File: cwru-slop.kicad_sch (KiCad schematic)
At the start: 24 parts, among them SW1 SW_SPDT, U1 TLV9001IDCK, U2 AP63205WU, U3 TLV75533PDBV, U4 STM32L433CCTx, U5 TPS2116DRL

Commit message: add accelerometer
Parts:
- added C16: 0.1u, Capacitor_SMD:C_0603_1608Metric_Pad1.08x0.95mm_HandSolder, symbol slopp:C
- added C17: 1.0u, Capacitor_SMD:C_0603_1608Metric_Pad1.08x0.95mm_HandSolder, symbol slopp:C
- added R2, R3: 4.7k, Resistor_SMD:R_0603_1608Metric_Pad0.98x0.95mm_HandSolder, symbol slopp:R
- added U6: FXLS8974CFR3, SYS27_Footprints:DFN10_2X2_STM, symbol slopp:FXLS8974CFR3
- C9: value 100n -> 0.1u
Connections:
- net GND is gone; now on net +3V3: C1.2, C10.2, C12.2, C13.1, C14.2, C15.2, C2.2, C3.2, C4.2, C5.2, C6.2, C7.2, C8.2, C9.1, SW1.1 (A), U2.4 (GND), U3.2 (GND), U4.23 (VSS), U4.35 (VSS), U4.47 (VSS), U4.8 (VSSA), U5.1 (GND)
- net +3V3: now also C16.1, C16.2, C17.1, C17.2, R2.2, R3.2, U6.1 (VDD), U6.10 (GND), U6.2 (BT_MODE), U6.9 (INTF_SEL)
- net +5V: no longer C12.1, C13.2, L1.2, U2.1 (FB), U5.3 (VIN1), U5.5 (MODE), U5.6 (VIN2)
- net ACCEL_SCL: now reaches U4.30 (PA9)
- net ACCEL_SCL: now also R2.1, U6.5 (SCL/SCLK)
- net ACCEL_SDA: now reaches U4.31 (PA10)
- net ACCEL_SDA: now also R3.1, U6.4 (SDA/SPI_MOSI/SPI_DATA)
- net BUCK_BST renamed BUCK_SW
- new net +5V_PWR: C12.1, C13.2, L1.2, U2.1 (FB), U5.3 (VIN1), U5.5 (MODE)
- new net +5V_USB: U5.6 (VIN2)
- no-connect marks 0 -> 4
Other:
- note added: "3V3 LDO"
- note added: "5V BUCK"
- note added: "5V PWR MUX"
- note added: "Accelerometer"
- note added: "POWER!"
- moved on the sheet: C10, C11, C12, C13, C14, C15, C9, L1, SW1, U1, U2, U3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

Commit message: can trans + esd prot
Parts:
- added C18, C19: 0.1u, Capacitor_SMD:C_0603_1608Metric_Pad1.08x0.95mm_HandSolder, symbol slopp:C
- added U7: ESDCAN24-2BLY, SYS27_Footprints:SOT_24-2BLY_STM, symbol slopp:ESDCAN24-2BLY
- added U8: MCP2562-E-SN, Package_SO:SOIC-8_3.9x4.9mm_P1.27mm, symbol slopp:MCP2562-E-SN
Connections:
- net +3.3V: now also C19.2, U8.5 (Vio)
- net +3V3: now also C18.2, C19.1, U7.3, U8.2 (VSS)
- net +5V: now also C18.1, U8.3 (VDD)
- net CAN_RXD: now reaches U4.32 (PA11)
- net CAN_RXD: now also U8.4 (RXD)
- net CAN_TXD: now reaches U4.33 (PA12)
- net CAN_TXD: now also U8.1 (TXD)
- net CAN_STBY: now reaches U4.34 (PA13)
- net CAN_STBY: now also U8.8 (STBY)
- new net: U7.2, U8.6 (CANL)
- new net: U7.1, U8.7 (CANH)
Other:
- note added: "CAN Transciever (to bus)"
- moved on the sheet: C16, C17, C8, FB1, R2, R3, U6

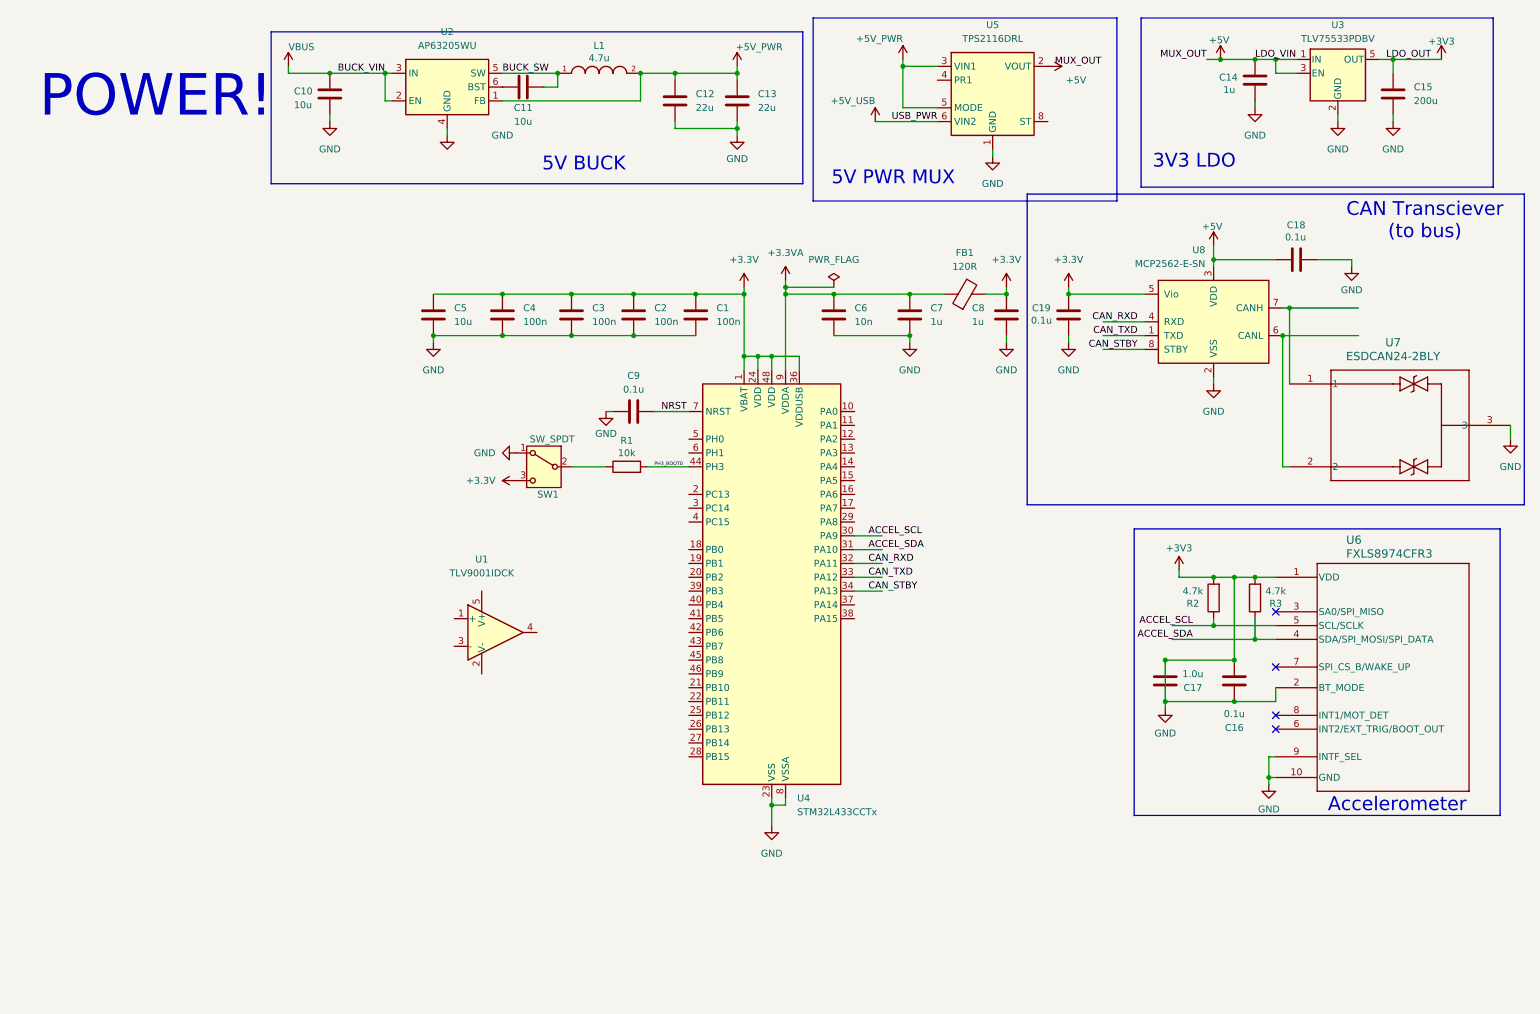
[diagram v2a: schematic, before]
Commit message: add eeprom and crystal
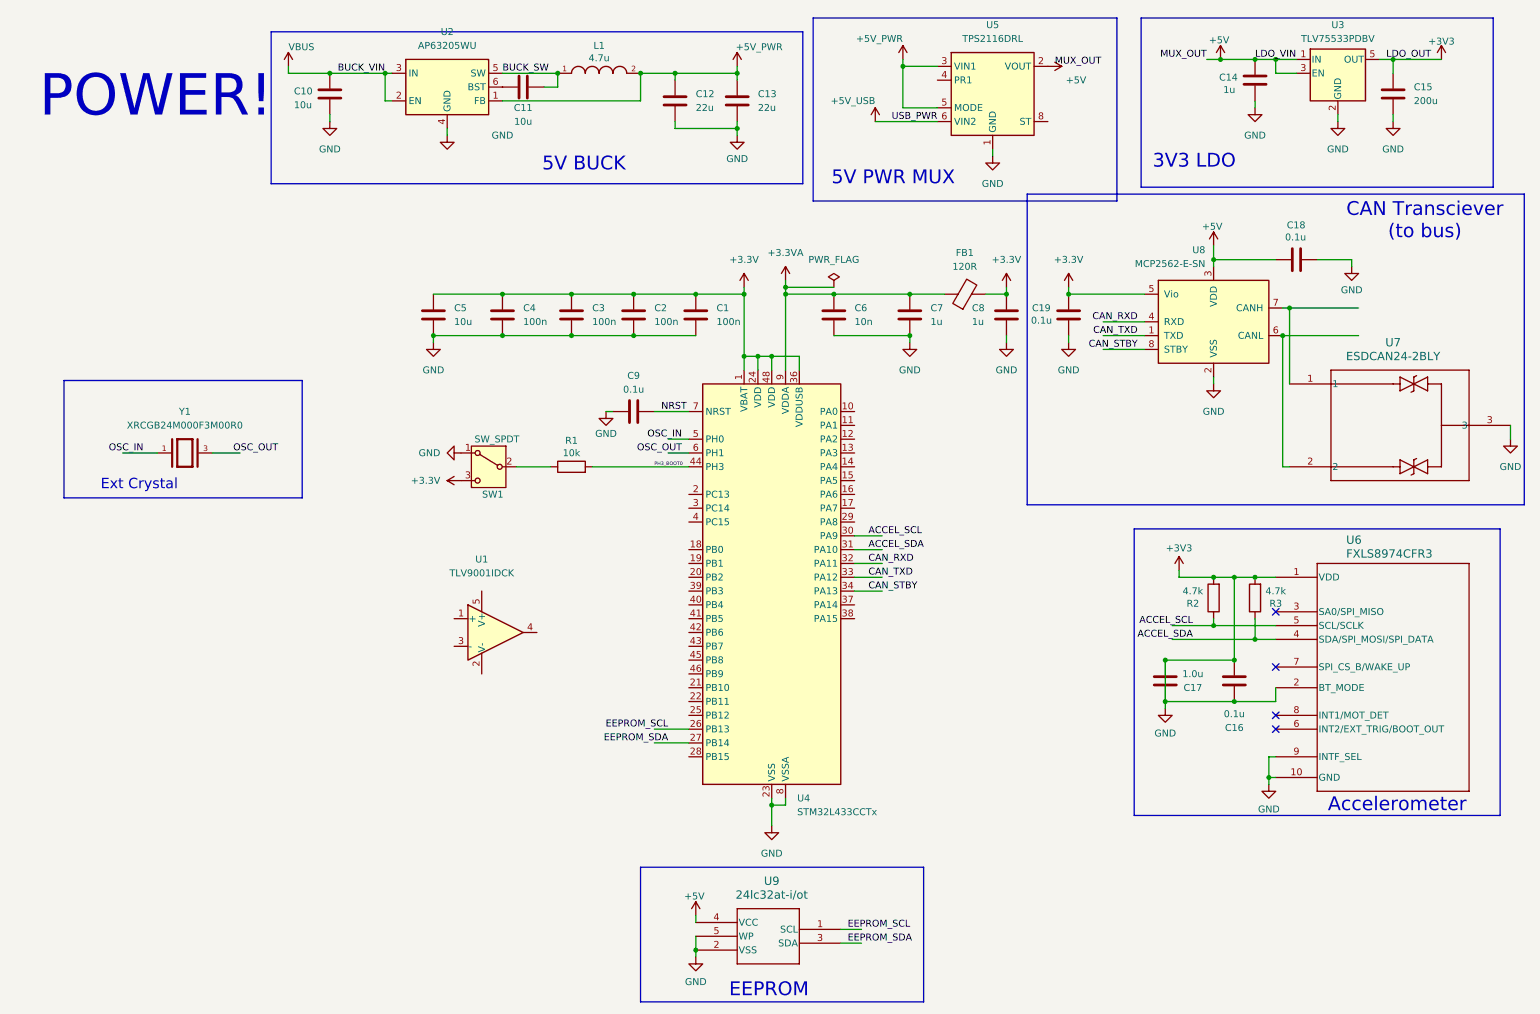
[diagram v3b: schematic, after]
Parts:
- added U9: 24lc32at-i/ot, SYS27_Footprints:SOT-24-5_MC_MCH, symbol slopp:24lc32at-i_ot
- added Y1: XRCGB24M000F3M00R0, SYS27_Footprints:OSC_XRCGB24M000F3M00R0, symbol slopp:XRCGB24M000F3M00R0
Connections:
- net +3V3: now also U9.2 (VSS), U9.5 (WP)
- net +5V: now also U9.4 (VCC)
- net EEPROM_SCL: now reaches U4.26 (PB13)
- net EEPROM_SCL: now also U9.1 (SCL)
- net EEPROM_SDA: now reaches U4.27 (PB14)
- net EEPROM_SDA: now also U9.3 (SDA)
- net OSC_IN: now reaches U4.5 (PH0)
- net OSC_IN: now also Y1.1
- net OSC_OUT: now reaches U4.6 (PH1)
- net OSC_OUT: now also Y1.3
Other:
- note added: "EEPROM"
- note added: "Ext Crystal"
- moved on the sheet: R1, SW1

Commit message: reorg i/o sides, add reset button
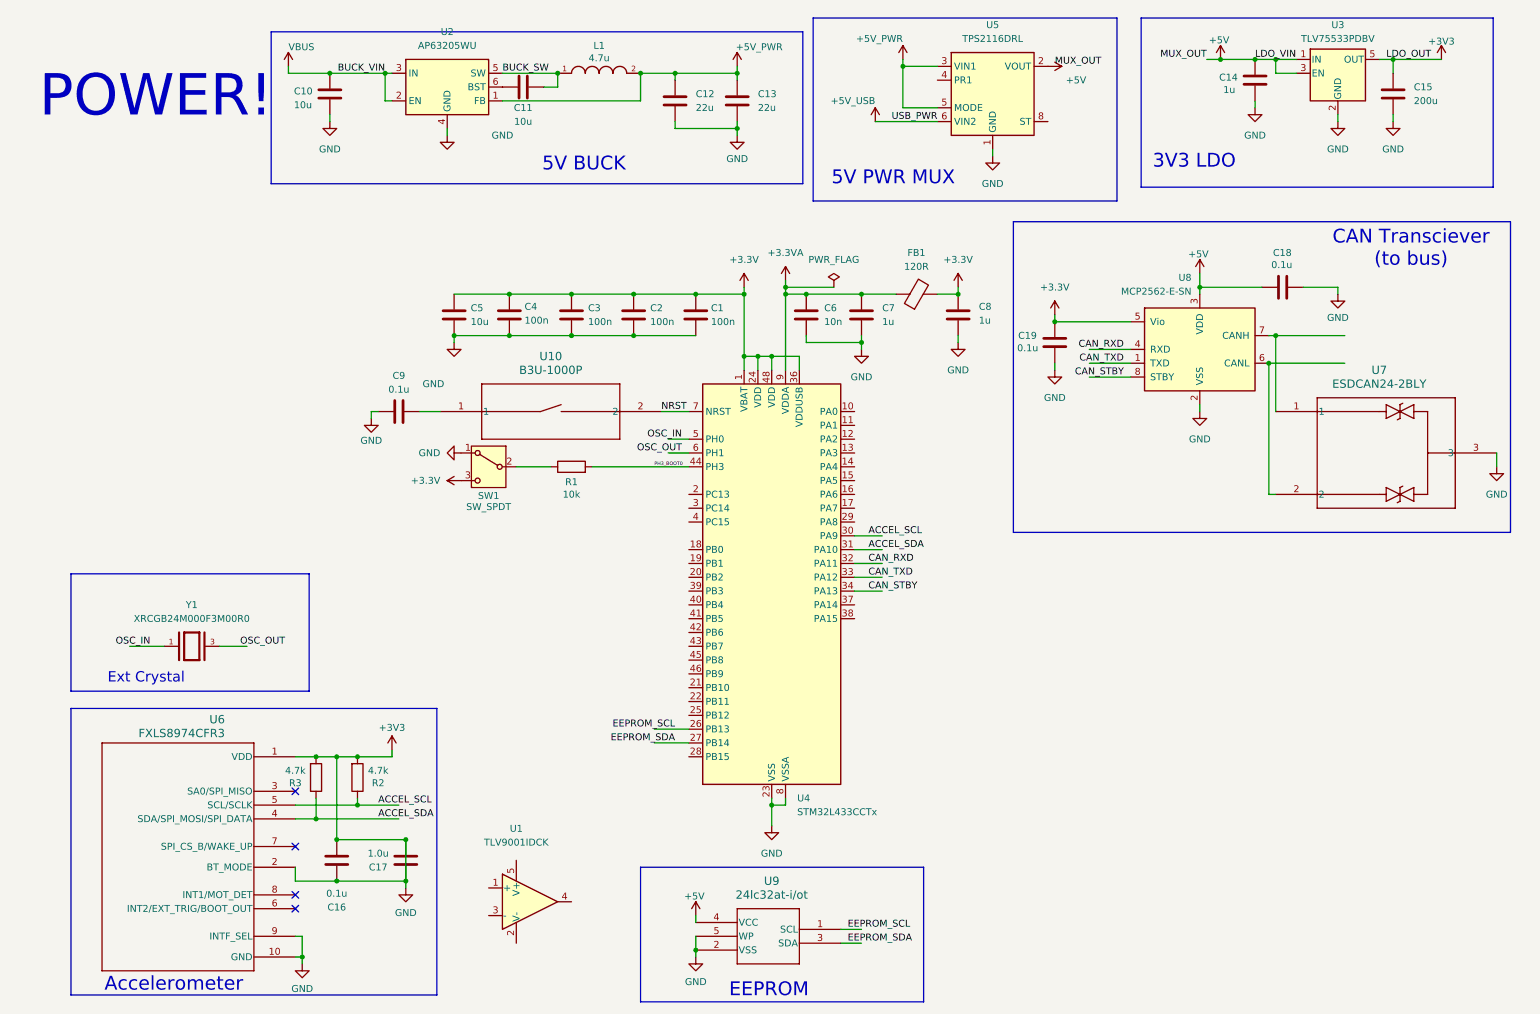
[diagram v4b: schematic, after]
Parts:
- added U10: B3U-1000P, SYS27_Footprints:B3U-1000P, symbol slopp:B3U-1000P
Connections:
- net NRST: now also U10.2; no longer C9.2
- new net: C9.2, U10.1
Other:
- moved on the sheet: C16, C17, C18, C19, C4, C5, C6, C7, C8, C9, FB1, R2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

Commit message: add usb-c 2.0 conn
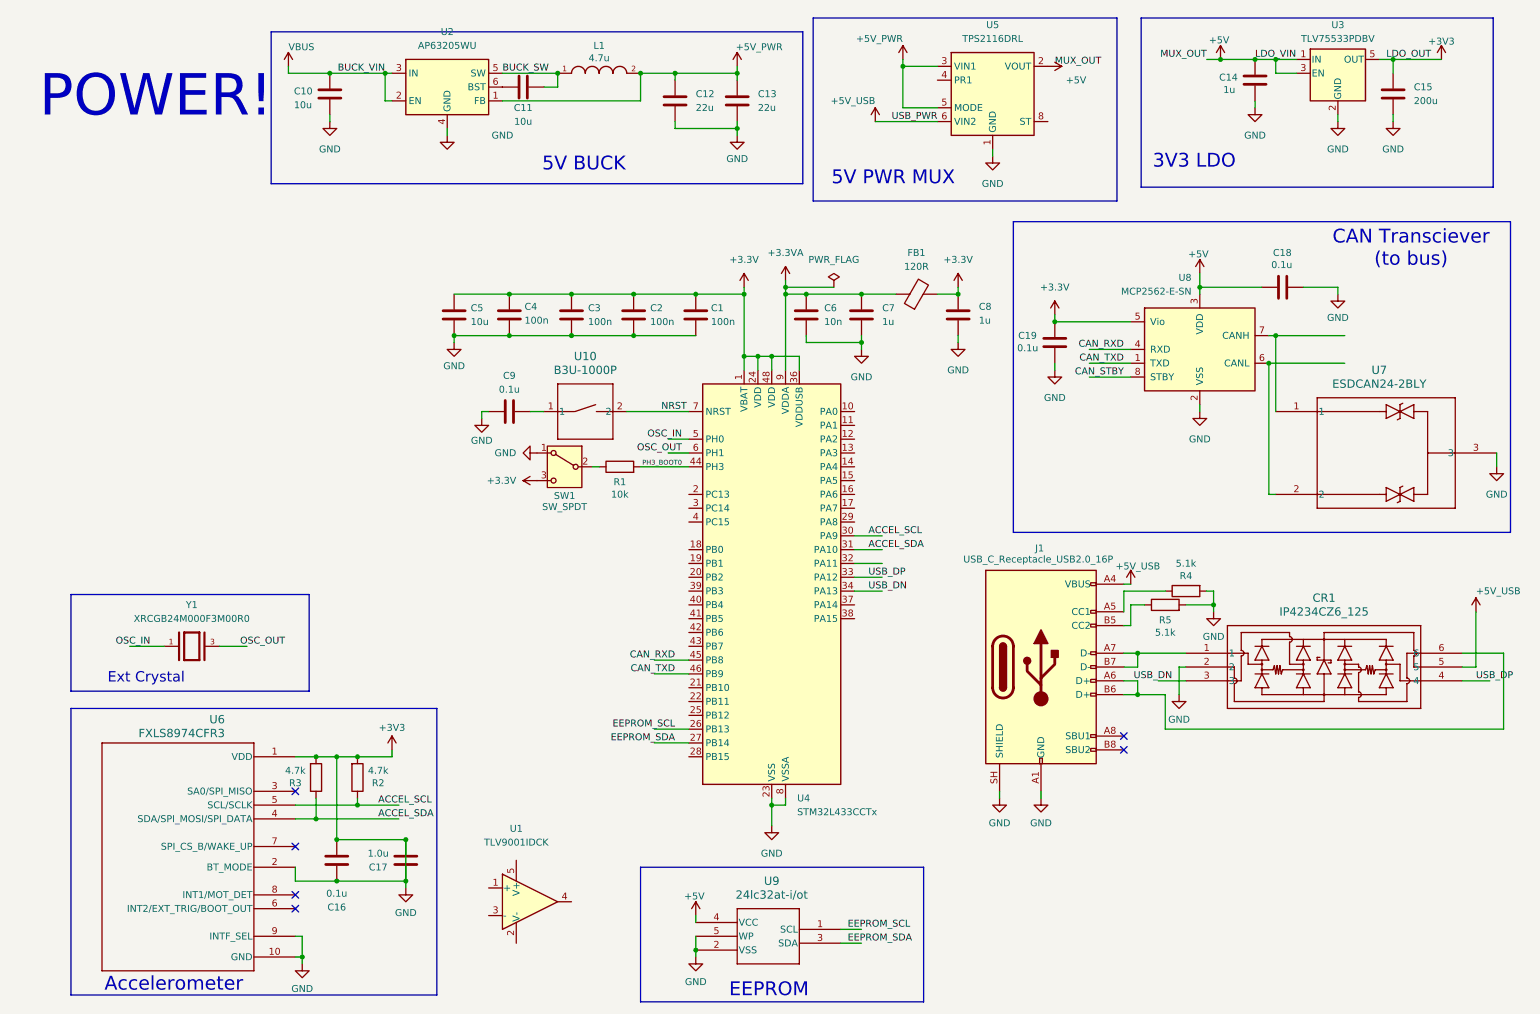
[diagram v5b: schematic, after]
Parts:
- added CR1: IP4234CZ6_125, SYS27_Footprints:TSOP6_SOT457_NEX, symbol slopp:IP4234CZ6_125
- added J1: USB_C_Receptacle_USB2.0_16P, SYS27_Footprints:B3U-1000P, symbol Connector:USB_C_Receptacle_USB2.0_16P
- added R4, R5: 5.1k, Resistor_SMD:R_0603_1608Metric_Pad0.98x0.95mm_HandSolder, symbol slopp:R
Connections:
- net +3V3: now also CR1.2, J1.A1 (GND), J1.A12 (GND), J1.B1 (GND), J1.B12 (GND), J1.SH (SHIELD), R4.2, R5.2
- net +5V_USB: now also CR1.5, J1.A4 (VBUS), J1.A9 (VBUS), J1.B4 (VBUS), J1.B9 (VBUS)
- net CAN_RXD: now also U4.45 (PB8); no longer U4.32 (PA11)
- net CAN_STBY: no longer U4.34 (PA13)
- net CAN_TXD: now also U4.46 (PB9); no longer U4.33 (PA12)
- new net: CR1.1, J1.A7 (D-), J1.B7 (D-)
- new net: CR1.6, J1.A6 (D+), J1.B6 (D+)
- new net: J1.B5 (CC2), R5.1
- new net: J1.A5 (CC1), R4.1
- new net USB_DN: CR1.3, U4.34 (PA13)
- new net USB_DP: CR1.4, U4.33 (PA12)
- no-connect marks 4 -> 6
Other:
- moved on the sheet: C9, R1, SW1, U10

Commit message: rotate usb diode, org
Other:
- note added: "USB w/ ESD"
- moved on the sheet: C1, C16, C17, C18, C19, C2, C3, C4, C5, C6, C7, C8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

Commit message: connect transciever stby to mcu
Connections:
- net CAN_STBY: now also U4.21 (PB10)
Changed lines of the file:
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@@
+	(wire
+		(pts
+			(xy 152.4 132.08) (xy 158.75 132.08)
+		)
+		(stroke
+			(width 0)
+			(type default)
+		)
+	)
 	(wire
 		(pts
@@
 		)
 	)
+	(label "CAN_STBY"
+		(at 156.21 132.08 180)
+		(effects
+			(font
+				(size 1.27 1.27)
+			)
+			(justify right bottom)
+		)
+	)

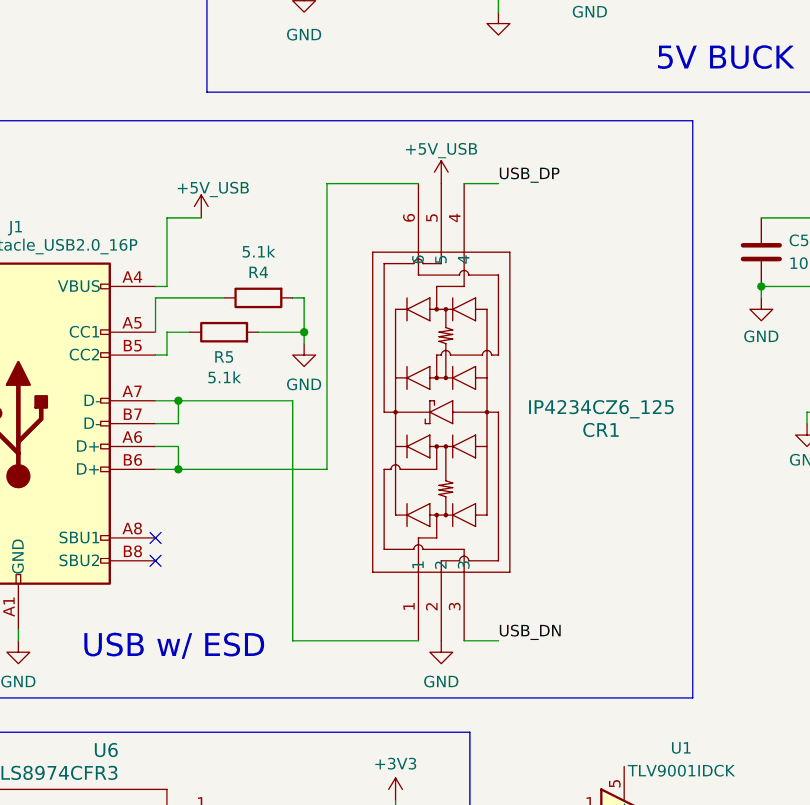
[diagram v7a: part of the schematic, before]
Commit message: reroute usb -> esd less confusingly
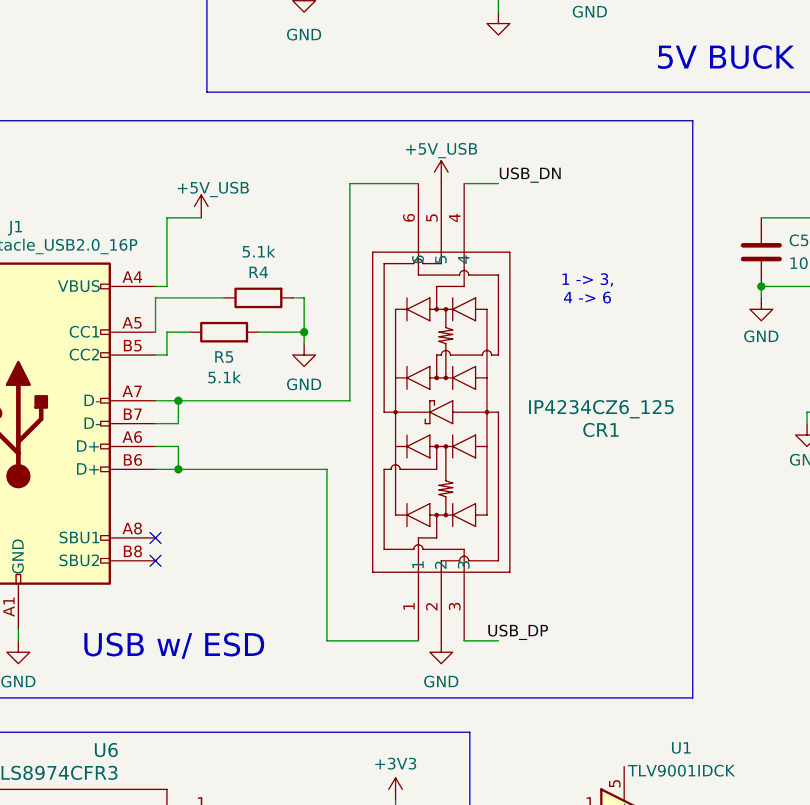
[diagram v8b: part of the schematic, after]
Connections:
- net USB_DN: now also CR1.4; no longer CR1.3
- net USB_DP: now also CR1.3; no longer CR1.4
- net at J1.A7 (D-), J1.B7 (D-): now also CR1.6; no longer CR1.1
- net at J1.A6 (D+), J1.B6 (D+): now also CR1.1; no longer CR1.6
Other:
- note added: "1 -> 3, 4 -> 6"
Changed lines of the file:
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@@
+		)
+	)
+	(text "1 -> 3,\n4 -> 6"
+		(exclude_from_sim no)
+		(at 96.266 67.818 0)
+		(effects
+			(font
+				(size 1.27 1.27)
+			)
 		)
 	)
@@
 	(wire
 		(pts
+			(xy 69.85 80.01) (xy 69.85 55.88)
+		)
+		(stroke
+			(width 0)
+			(type default)
+		)
+	)
+	(wire
+		(pts
 			(xy 115.57 59.69) (xy 168.91 59.69)
 		)
@@
 	(wire
 		(pts
-			(xy 63.5 106.68) (xy 77.47 106.68)
-		)
-		(stroke
-			(width 0)
-			(type default)
-		)
-	)
-	(wire
-		(pts
-			(xy 50.8 80.01) (xy 63.5 80.01)
+			(xy 50.8 80.01) (xy 69.85 80.01)
 		)
 		(stroke
@@
 	(wire
 		(pts
-			(xy 67.31 87.63) (xy 67.31 55.88)
-		)
-		(stroke
-			(width 0)
-			(type default)
-		)
-	)
-	(wire
-		(pts
 			(xy 158.75 185.42) (xy 162.56 185.42)
 		)
@@
 	(wire
 		(pts
+			(xy 69.85 55.88) (xy 77.47 55.88)
+		)
+		(stroke
+			(width 0)
+			(type default)
+		)
+	)
+	(wire
+		(pts
 			(xy 173.99 153.67) (xy 173.99 152.4)
 		)
@@
 	(wire
 		(pts
+			(xy 67.31 87.63) (xy 67.31 106.68)
+		)
+		(stroke
+			(width 0)
+			(type default)
+		)
+	)
+	(wire
+		(pts
 			(xy 257.81 116.84) (xy 264.16 116.84)
 		)
@@
 	(wire
 		(pts
-			(xy 67.31 55.88) (xy 77.47 55.88)
-		)
-		(stroke
-			(width 0)
-			(type default)
-		)
-	)
-	(wire
-		(pts
 			(xy 238.76 22.86) (xy 242.57 22.86)
 		)
@@
 	(wire
 		(pts
-			(xy 63.5 80.01) (xy 63.5 106.68)
-		)
-		(stroke
-			(width 0)
-			(type default)
-		)
-	)
-	(wire
-		(pts
 			(xy 96.52 25.4) (xy 106.68 25.4)
 		)
@@
 	(wire
 		(pts
+			(xy 67.31 106.68) (xy 77.47 106.68)
+		)
+		(stroke
+			(width 0)
+			(type default)
+		)
+	)
+	(wire
+		(pts
 			(xy 50.8 82.55) (xy 48.26 82.55)
 		)
@@
 	)
 	(label "USB_DP"
-		(at 86.36 55.88 0)
+		(at 85.09 106.68 0)
 		(effects
 			(font
@@
 	(label "ACCEL_SCL"
 		(at 72.39 134.62 0)
-		(effects
-			(font
-				(size 1.27 1.27)
-			)
-			(justify left bottom)
-		)
-	)
-	(label "USB_DN"
-		(at 86.36 106.68 0)
 		(effects
 			(font
@@
 		(effects
 			(font
+				(size 1.27 1.27)
+			)
+			(justify left bottom)
+		)
+	)
+	(label "USB_DN"
+		(at 86.36 55.88 0)
+		(effects
+			(font
